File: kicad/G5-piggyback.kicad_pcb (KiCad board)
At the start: 2 copper layers, 77.5 x 15.3 mm, 5 parts, among them SW1 KSC241GLFS, SW2 RotaryEncoder_Switch_MP, X1 microSD_Card

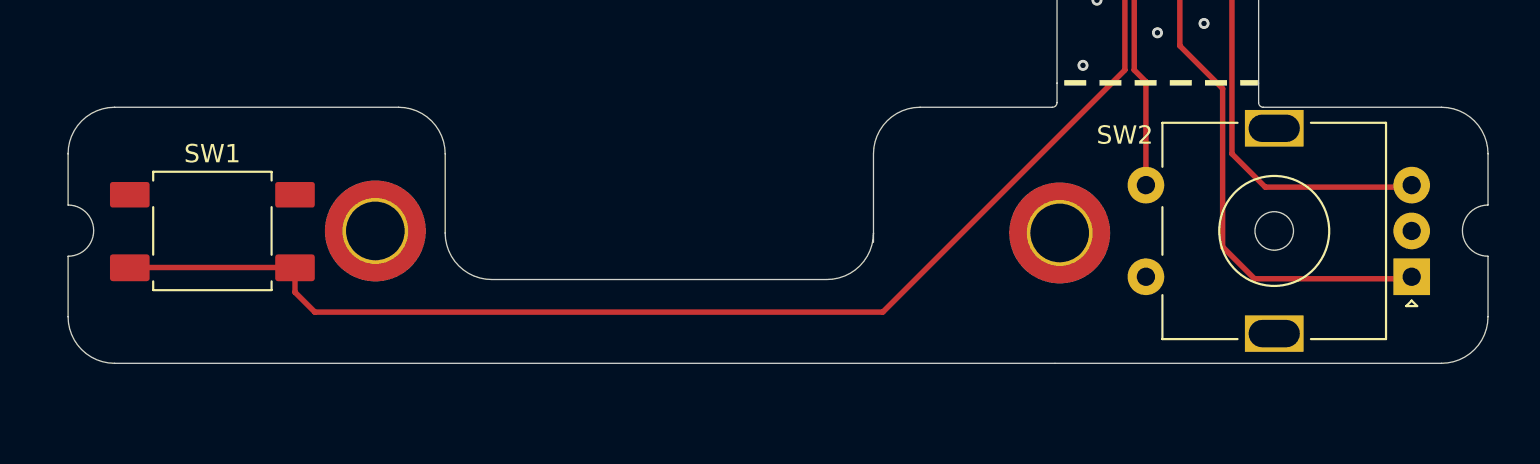
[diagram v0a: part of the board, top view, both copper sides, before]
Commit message: Updated layout slightly: centered things vertically, added slightly more space between devboard case and pcb top edge so the microsd click mechanism can hopefully operate without disassembly.
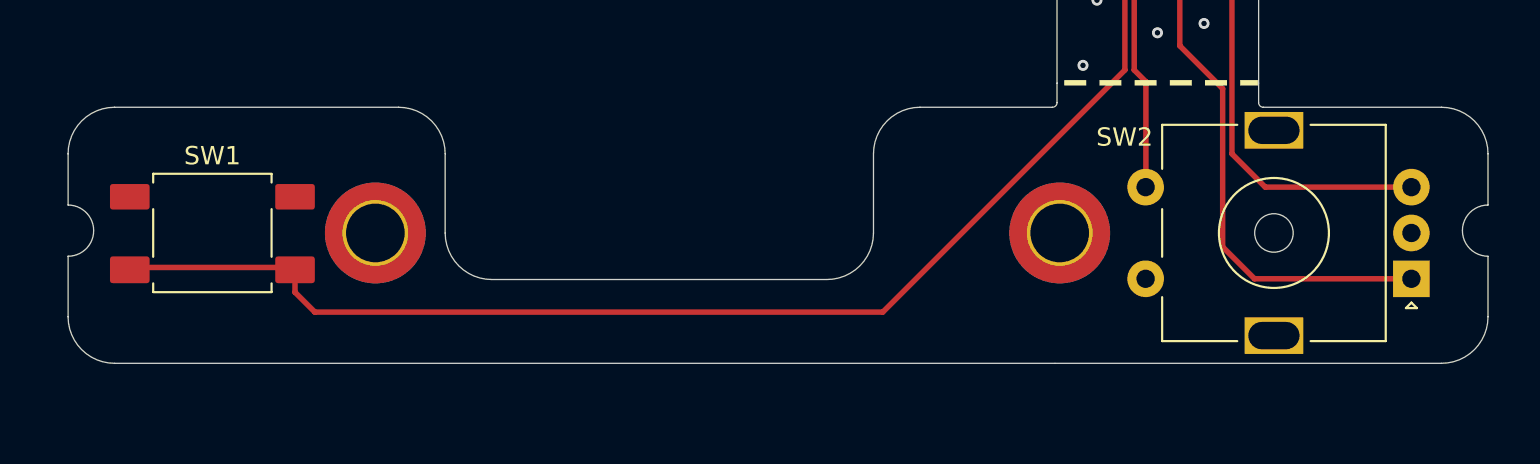
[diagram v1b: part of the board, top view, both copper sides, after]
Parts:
- moved SW2 0.11 mm to (136.3, 165.1)
- moved H1 0.11 mm to (79.8, 162.6)
- moved SW1 0.11 mm to (70.9, 162.6)
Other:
- outline, holes or cut-outs redrawn
